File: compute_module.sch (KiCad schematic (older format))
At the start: 18 parts, among them Q1 2N7002P.215

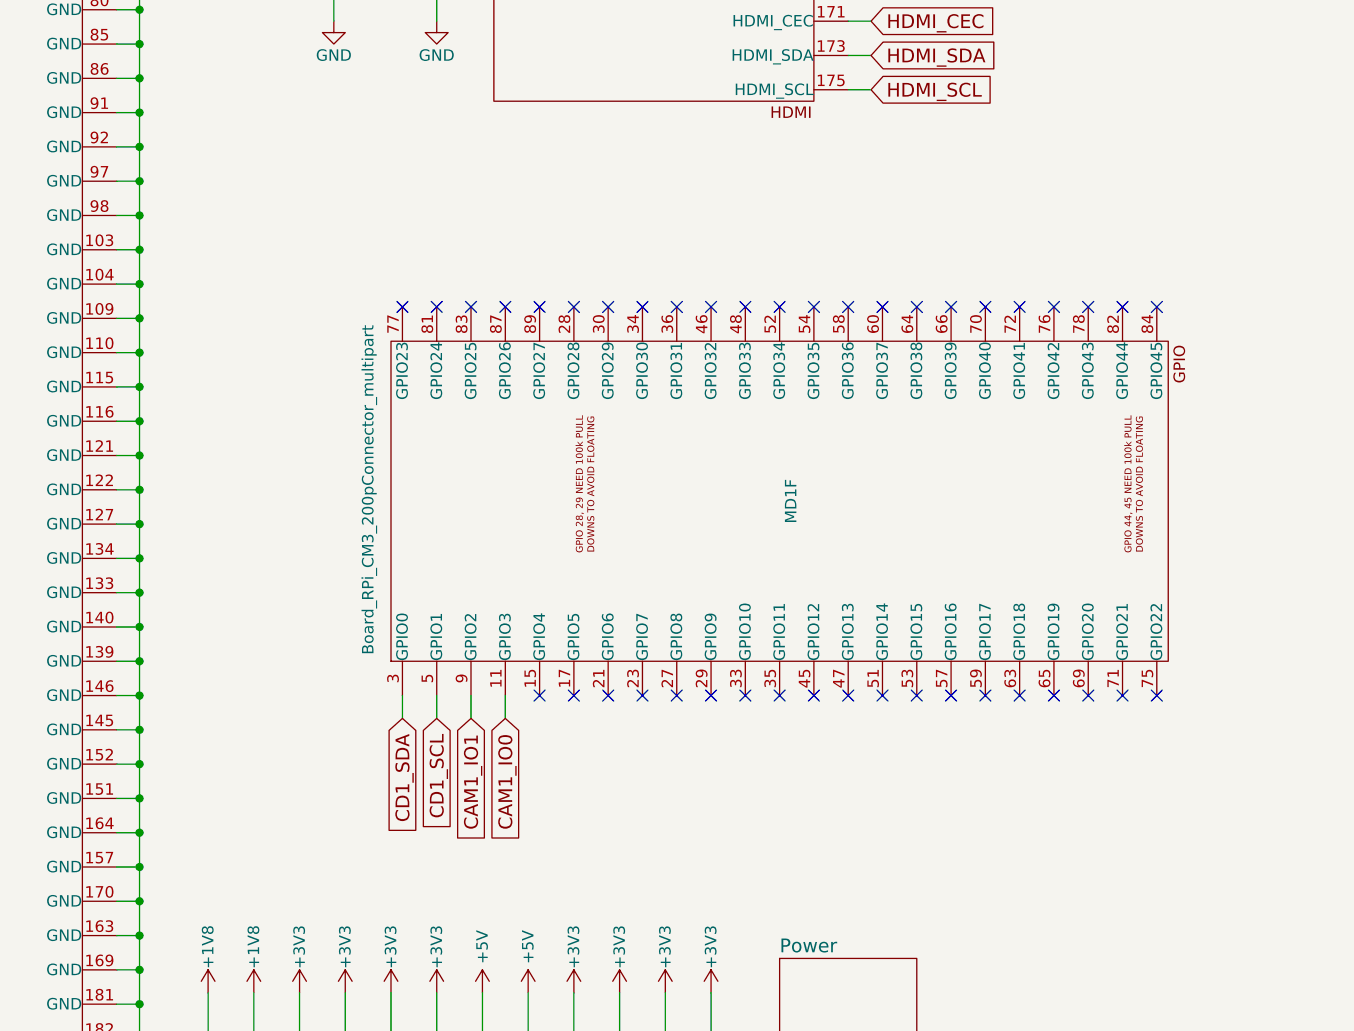
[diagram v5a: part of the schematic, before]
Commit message: Added pull-ups for gpio28, 29, 44 and 45
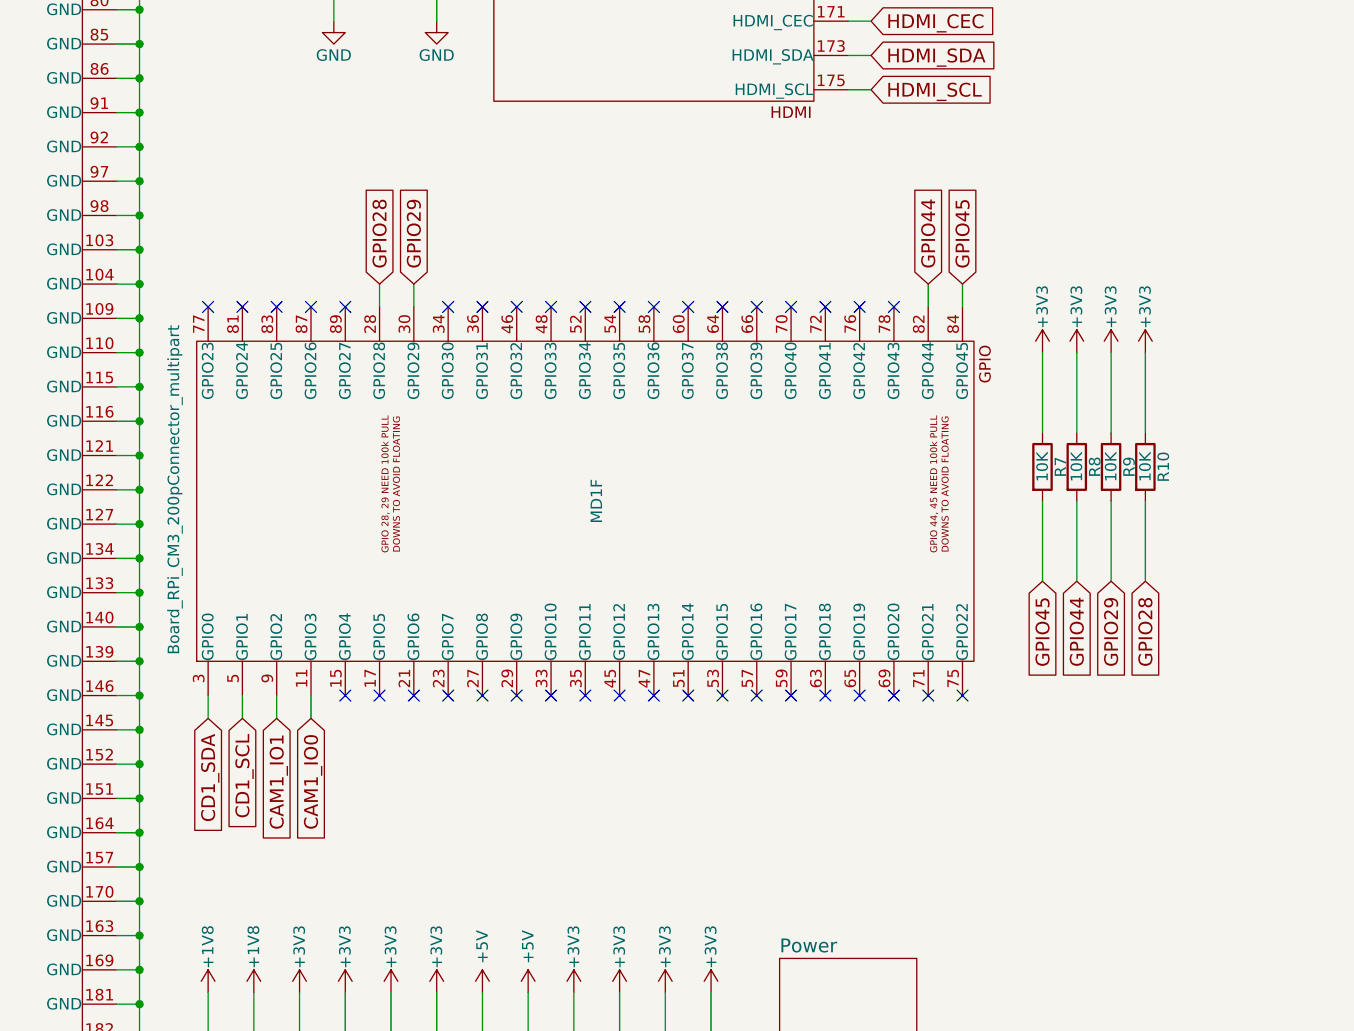
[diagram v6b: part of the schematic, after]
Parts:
- added R10, R7, R8, R9: 10K, Resistors_SMD:R_0603_HandSoldering, symbol R
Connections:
- net +3V3: now also R10.1, R7.1, R8.1, R9.1
- net GPIO28: now reaches MD1.28 (GPIO28)
- net GPIO28: now also R10.2
- net GPIO29: now reaches MD1.30 (GPIO29)
- net GPIO29: now also R9.2
- net GPIO44: now reaches MD1.82 (GPIO44)
- net GPIO44: now also R8.2
- net GPIO45: now reaches MD1.84 (GPIO45)
- net GPIO45: now also R7.2
- no-connect marks 72 -> 68
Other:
- moved on the sheet: MD1F

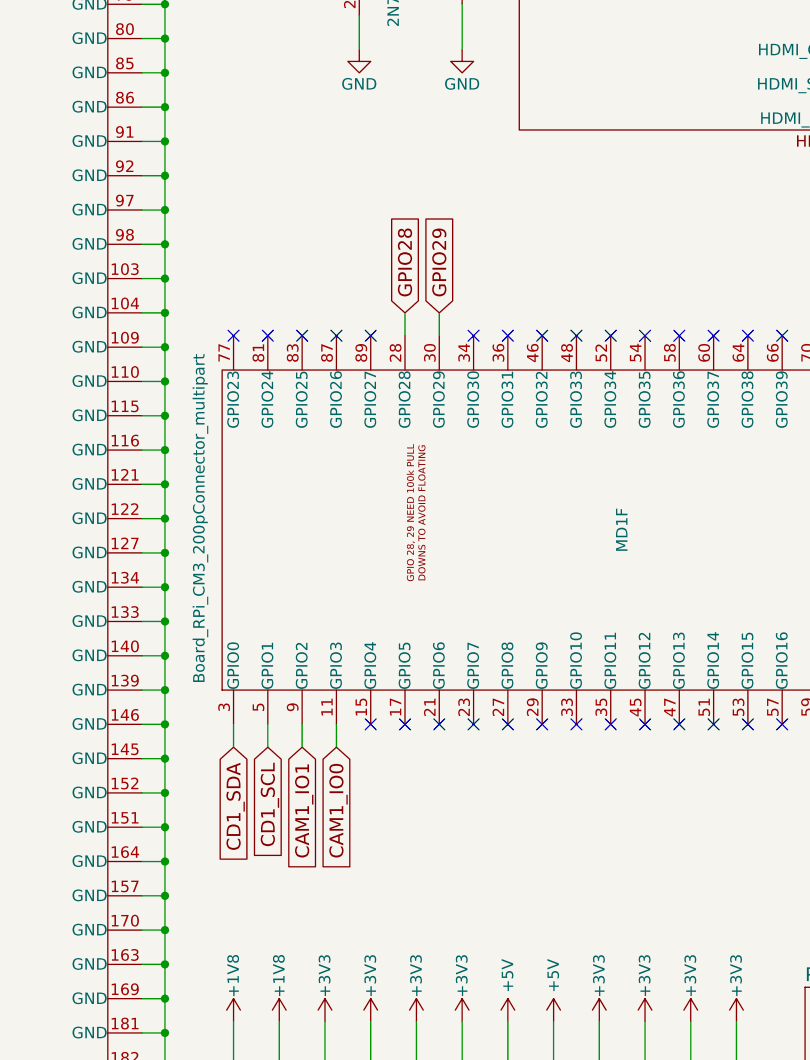
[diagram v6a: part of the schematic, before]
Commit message: Moved CAM1_IO0 and CAM1_IO1 to gpio 31 and 30
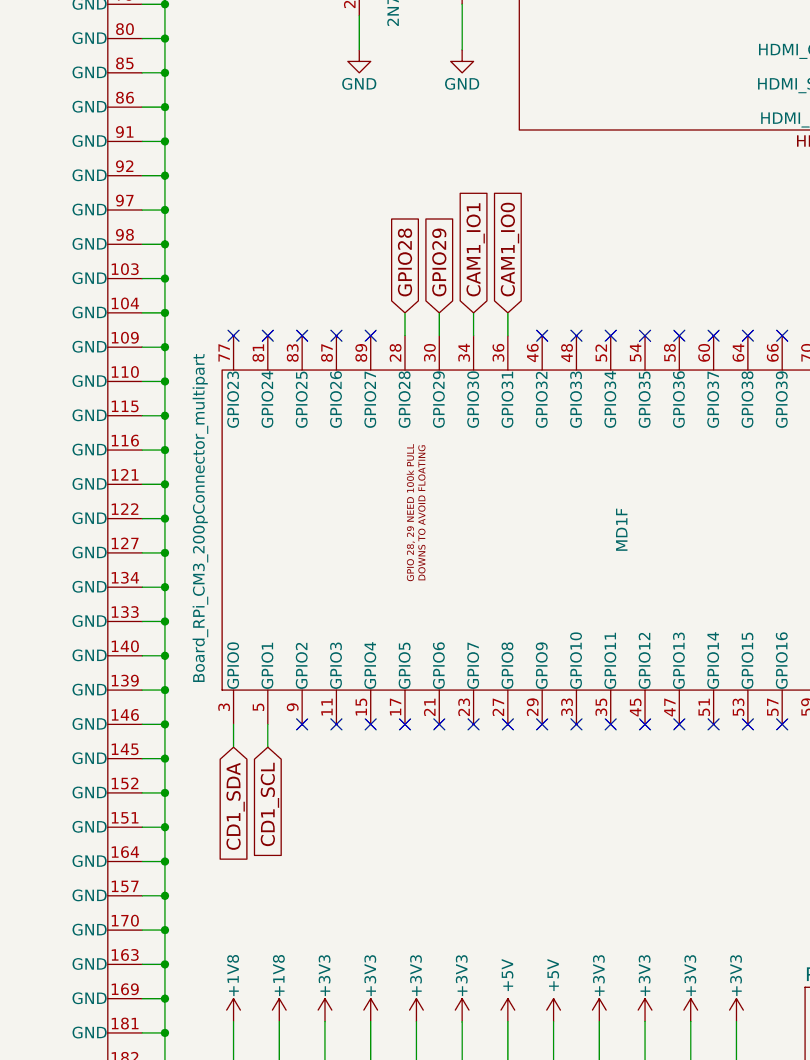
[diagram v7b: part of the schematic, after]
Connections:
- net CAM1_IO0: now also MD1.36 (GPIO31); no longer MD1.11 (GPIO3)
- net CAM1_IO1: now also MD1.34 (GPIO30); no longer MD1.9 (GPIO2)
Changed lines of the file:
@@
 Text GLabel 3700 5450 3    60   Input ~ 0
 CD1_SCL
-Text GLabel 3850 5450 3    60   Input ~ 0
+Text GLabel 4600 3550 1    60   Input ~ 0
 CAM1_IO1
-Text GLabel 4000 5450 3    60   Input ~ 0
+Text GLabel 4750 3550 1    60   Input ~ 0
 CAM1_IO0
 Text GLabel 9400 5000 0    60   Input ~ 0
@@
 Wire Wire Line
 	3700 5350 3700 5450
-Wire Wire Line
-	3850 5350 3850 5450
-Wire Wire Line
-	4000 5350 4000 5450
 Wire Wire Line
 	9500 5000 9400 5000
@@
 NoConn ~ 5050 3650
 NoConn ~ 4900 3650
-NoConn ~ 4750 3650
-NoConn ~ 4600 3650
 NoConn ~ 4150 3650
 NoConn ~ 4000 3650
@@
 	1    0    0    -1
 $EndComp
+NoConn ~ 3850 5350
+NoConn ~ 4000 5350
+Wire Wire Line
+	4600 3550 4600 3650
+Wire Wire Line
+	4750 3550 4750 3650
 $EndSCHEMATC

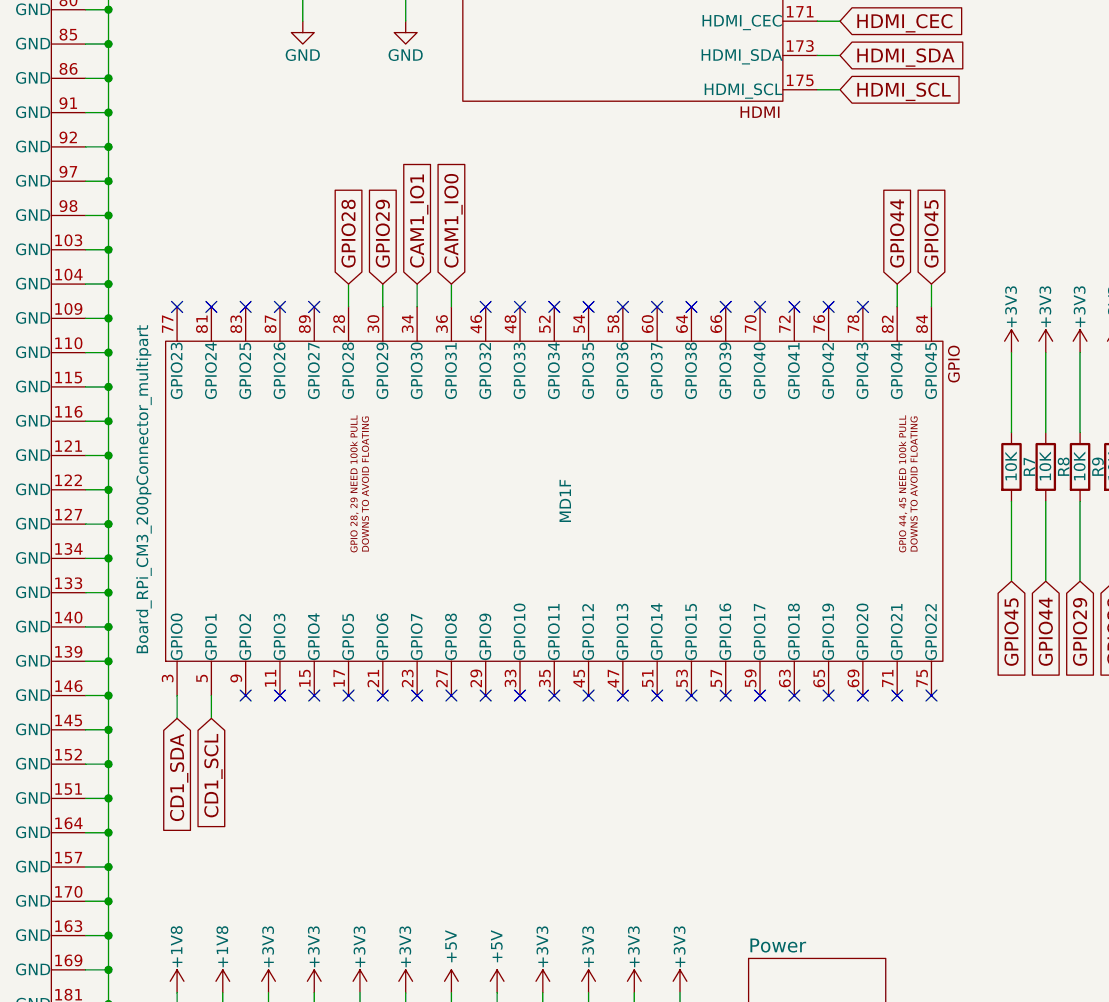
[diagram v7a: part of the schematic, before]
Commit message: Partially routed gpio header
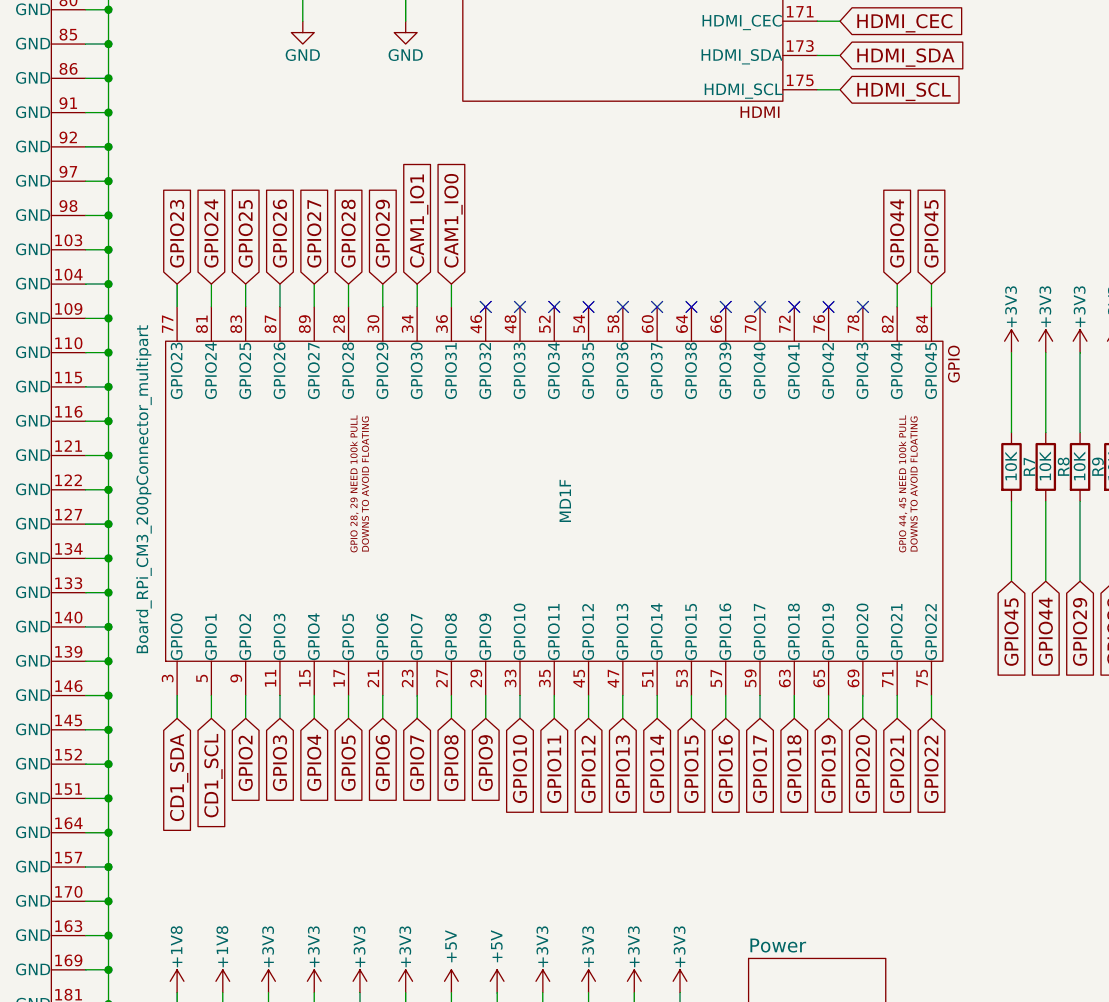
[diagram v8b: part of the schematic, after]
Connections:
- net GPIO3: now reaches MD1.11 (GPIO3)
- net GPIO4: now reaches MD1.15 (GPIO4)
- net GPIO5: now reaches MD1.17 (GPIO5)
- net GPIO6: now reaches MD1.21 (GPIO6)
- net GPIO7: now reaches MD1.23 (GPIO7)
- net GPIO8: now reaches MD1.27 (GPIO8)
- net GPIO9: now reaches MD1.29 (GPIO9)
- net GPIO10: now reaches MD1.33 (GPIO10)
- net GPIO11: now reaches MD1.35 (GPIO11)
- net GPIO12: now reaches MD1.45 (GPIO12)
- net GPIO13: now reaches MD1.47 (GPIO13)
- net GPIO14: now reaches MD1.51 (GPIO14)
- net GPIO15: now reaches MD1.53 (GPIO15)
- net GPIO16: now reaches MD1.57 (GPIO16)
- net GPIO17: now reaches MD1.59 (GPIO17)
- net GPIO18: now reaches MD1.63 (GPIO18)
- net GPIO19: now reaches MD1.65 (GPIO19)
- net GPIO20: now reaches MD1.69 (GPIO20)
- net GPIO21: now reaches MD1.71 (GPIO21)
- net GPIO22: now reaches MD1.75 (GPIO22)
- net GPIO23: now reaches MD1.77 (GPIO23)
- net GPIO24: now reaches MD1.81 (GPIO24)
- net GPIO25: now reaches MD1.83 (GPIO25)
- net GPIO26: now reaches MD1.87 (GPIO26)
- net GPIO27: now reaches MD1.89 (GPIO27)
- net GPIO2: now reaches MD1.9 (GPIO2)
- no-connect marks 68 -> 42
